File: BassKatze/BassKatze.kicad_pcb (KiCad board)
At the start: 2 copper layers, 55 x 54.9 mm, 52 parts, among them J1 Conn_01x02_Female, Q1 IRF7404, Q2 BSS138, SW1 SW_Push, U1 ATmega328-AU, U2 MSGEQ7, U3 TP4056

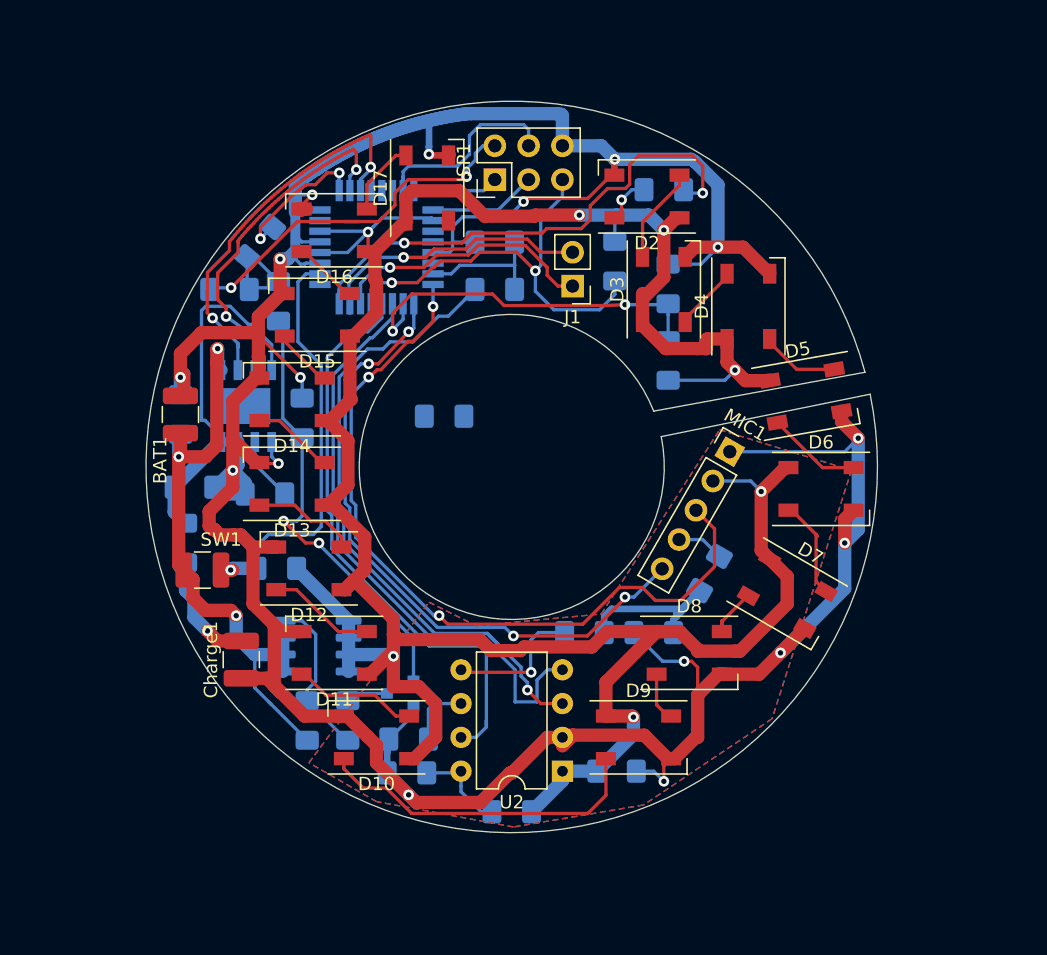
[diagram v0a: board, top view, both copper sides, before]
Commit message: use TP5400 to remove issues with isp voltage
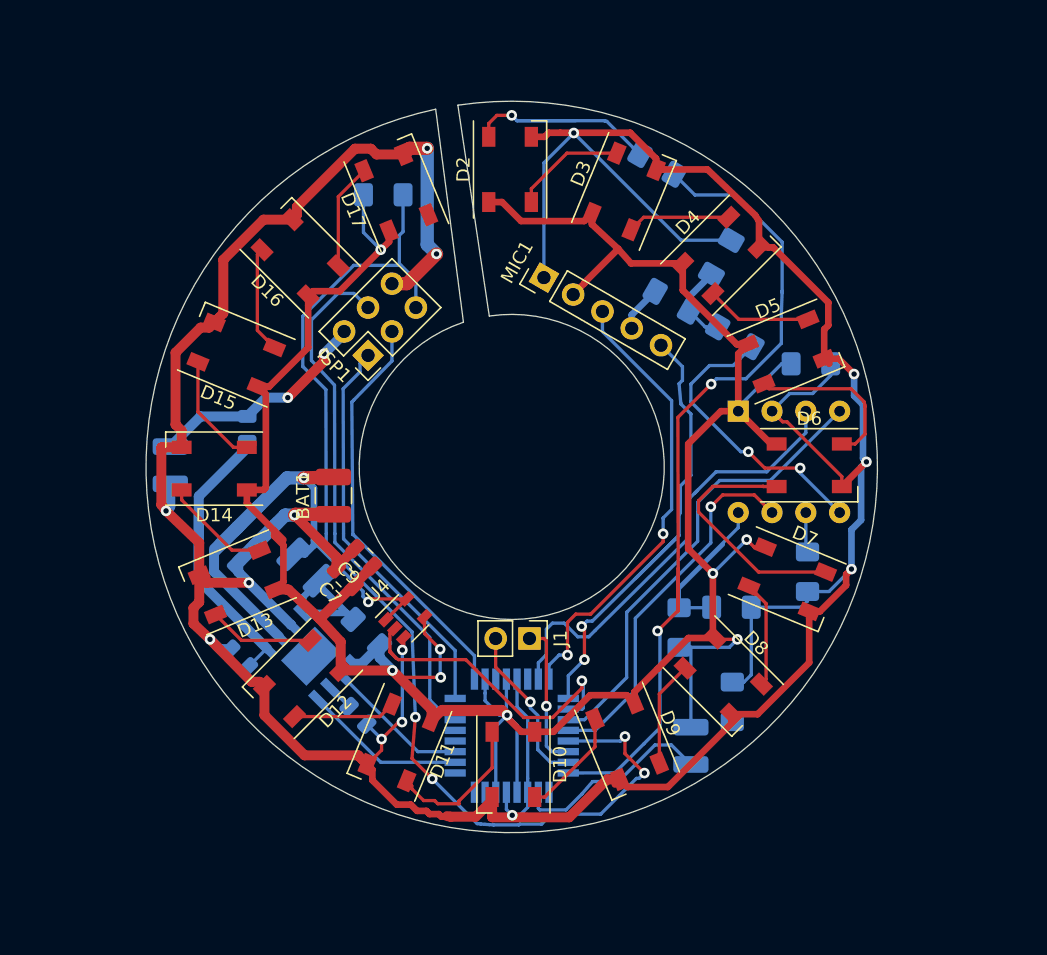
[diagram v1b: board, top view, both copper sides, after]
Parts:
- removed D18, D19: D, Diode_SMD:D_1206_3216Metric_Pad1.42x1.75mm_HandSolder
- removed Q1: IRF7404, Package_SO:SOIC-8_3.9x4.9mm_P1.27mm
- removed Q2: BSS138, Package_TO_SOT_SMD:SOT-23
- removed R10, R8: 5KOhm, Resistor_SMD:R_1206_3216Metric_Pad1.42x1.75mm_HandSolder
- removed R11, R12, R13: 10KOhm, Resistor_SMD:R_1206_3216Metric_Pad1.42x1.75mm_HandSolder
- removed R7, R9: 1KOhm, Resistor_SMD:R_1206_3216Metric_Pad1.42x1.75mm_HandSolder
- removed RProg1: 1.2kOhm, Resistor_SMD:R_1206_3216Metric_Pad1.42x1.75mm_HandSolder
- added C10: 22uF, Capacitor_SMD:C_0805_2012Metric, B.Cu at (105.7, 133.6)
- added C7: 0.1uF, Capacitor_SMD:C_0805_2012Metric, F.Cu at (114.5, 135.3)
- added C8: 22uF, Capacitor_SMD:C_0805_2012Metric, B.Cu at (107.1, 132.2)
- added C9: 47uF, Capacitor_SMD:C_0805_2012Metric, F.Cu at (115.9, 133.8)
- added L1: 10uH, Inductor_SMD:L_1210_3225Metric, B.Cu at (111.6, 134.6)
- added U4: TS5A3166DBVR, Package_TO_SOT_SMD:SOT-23-5, F.Cu at (119.0, 138.4)
- C1: footprint Resistor_SMD:R_1206_3216Metric_Pad1.42x1.75mm_HandSolder -> Capacitor_SMD:C_0805_2012Metric
- C2: value 10uF -> 0.1uF; footprint Resistor_SMD:R_1206_3216Metric_Pad1.42x1.75mm_HandSolder -> Capacitor_SMD:C_0805_2012Metric
- Charge1, SW1, U2: moved to B.Cu
- D1: value D -> 3A 20V; footprint Diode_SMD:D_1206_3216Metric_Pad1.42x1.75mm_HandSolder -> Diode_SMD:D_1206_3216Metric
- R1: value 0.4Ohm -> 0.2Ohm; footprint Resistor_SMD:R_1206_3216Metric_Pad1.42x1.75mm_HandSolder -> Resistor_SMD:R_0805_2012Metric
- R4: value 10KOhm -> 1.2KOhm; footprint Resistor_SMD:R_1206_3216Metric_Pad1.42x1.75mm_HandSolder -> Resistor_SMD:R_0805_2012Metric
- U3: value TP4056 -> TP5400
- moved SW1 39.0 mm to (140.5, 148.0), turned to 270 degrees
- moved U1 38.1 mm to (127.0, 147.2), turned to 90 degrees
- moved C5 33.9 mm to (149.5, 119.3)
- moved C6 32.5 mm to (149.2, 134.9), turned to 270 degrees
- moved R15 30.5 mm to (143.6, 144.7), turned to 270 degrees
- moved U2 30.1 mm to (144.0, 122.8), turned to 270 degrees
- moved R2 28.6 mm to (142.7, 111.3), turned to 240 degrees
- moved C4 27.4 mm to (143.5, 137.5), turned to 0 degrees
- moved J1 26.7 mm to (128.3, 139.9), turned to 270 degrees
- moved C3 24.9 mm to (143.8, 117.2), turned to 150 degrees
- moved R6 20.6 mm to (139.1, 114.6), turned to 150 degrees
- moved U3 19.4 mm to (111.9, 141.2), turned to 135 degrees
- moved MIC1 19.1 mm to (129.4, 112.8), turned to 60 degrees
- moved R3 18.7 mm to (139.6, 139.1), turned to 270 degrees
- moved R5 18.1 mm to (117.3, 106.6), turned to 0 degrees
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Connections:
- C1 pad 1: Net-(C1-Pad1) -> BAT-
- C1 pad 2: BAT- -> Net-(C1-Pad2)
- Charge1 pad 2: 5V_IN -> 5V_Flash
- D1 pad 2: Button -> Net-(D1-Pad2)
- D17 pad 4: Net-(D17-Pad4) -> (no net)
- R1 pad 1: 5V_IN -> Net-(C1-Pad2)
- R1 pad 2: Net-(C1-Pad1) -> 5V_Flash
- R4 pad 1: Net-(Q1-Pad4) -> BAT-
- R4 pad 2: BAT+ -> Net-(R4-Pad2)
- R5 pad 1: Reset -> PWR
- R5 pad 2: PWR -> Reset
- SW1 pad 1: BAT+ -> PWR
- U1 pad 1: Net-(U1-Pad1) -> (no net)
- U1 pad 10: CHRG -> STDBY
- U1 pad 11: STDBY -> CHRG
- U1 pad 12: Net-(U1-Pad12) -> (no net)
- U1 pad 13: Net-(U1-Pad13) -> (no net)
- U1 pad 14: Net-(U1-Pad14) -> (no net)
- U1 pad 19: Net-(U1-Pad19) -> (no net)
- U1 pad 20: Net-(U1-Pad20) -> PWR
- U1 pad 22: Net-(U1-Pad22) -> (no net)
- U1 pad 23: Net-(R10-Pad2) -> RAW_Spectrum
- U1 pad 26: Net-(R7-Pad1) -> BAT+_Switched
- U1 pad 7: Net-(U1-Pad7) -> (no net)
- U1 pad 8: Net-(U1-Pad8) -> (no net)
- U1 pad 9: PWR_HOLD -> (no net)
- U3 pad 1: BAT- -> PWR
- U3 pad 2: Net-(RProg1-Pad1) -> CHRG
- U3 pad 3: BAT- -> Net-(R4-Pad2)
- U3 pad 4: Net-(C1-Pad1) -> STDBY
- U3 pad 5: BAT+ -> Net-(C1-Pad2)
- U3 pad 6: STDBY -> BAT+
- U3 pad 7: CHRG -> BAT-
- U3 pad 8: Net-(C1-Pad1) -> Net-(D1-Pad2)
- U3 pad 9: Net-(U3-Pad9) -> (no net)
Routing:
- net Reset: track 32.4 -> 85.1 mm, vias 2 -> 4
- net Net-(Q2-Pad1): track 33.5 -> 0.00 mm, vias 2 -> 0
- net Net-(R7-Pad1): track 28.2 -> 0.00 mm, vias 2 -> 0
- net Net-(C1-Pad1): track 28.0 -> 0.00 mm
- net Net-(C1-Pad2): track 0.00 -> 26.4 mm
- net Gain_Select: track 59.3 -> 34.6 mm, vias 3 -> 2
- net Net-(R14-Pad2): track 39.2 -> 63.6 mm
- net MOSI: track 15.6 -> 39.9 mm
- net BAT+_Switched: track 0.00 -> 23.8 mm, vias 0 -> 1
- net MISO: track 6.43 -> 30.0 mm
- net SCK: track 8.12 -> 31.2 mm
- net BAT-: track 285.3 -> 306.6 mm, vias 16 -> 14
- net RAW_Spectrum: track 51.8 -> 34.0 mm, vias 1 -> 0
- net STDBY: track 29.8 -> 12.3 mm, vias 2 -> 0
- net Net-(D10-Pad2): track 25.1 -> 8.17 mm
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- removed copper zone on B.Cu, net BAT-
- removed copper zone on F.Cu, net BAT-
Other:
- board size 55 x 54.9 mm -> 55 x 55 mm
- board text removed: "BassKatze Rev 0.4"

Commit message: update of the layout
Signed-off-by: Kai Boernert <kai-boernert@visiongamestudios.de>
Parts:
- C3, C4, C5, C6, R14, R15, R2, R3, R5, R6: footprint Resistor_SMD:R_1206_3216Metric_Pad1.42x1.75mm_HandSolder -> Resistor_SMD:R_0805_2012Metric_Pad1.15x1.40mm_HandSolder
- R1: footprint Resistor_SMD:R_0805_2012Metric -> Resistor_SMD:R_1206_3216Metric_Pad1.42x1.75mm_HandSolder
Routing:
- net PWR: track 227.0 -> 237.6 mm
- net BAT-: track 306.6 -> 309.7 mm, vias 14 -> 15
- net RAW_Spectrum: track 34.0 -> 32.0 mm
- net Attack_Select: track 36.5 -> 35.6 mm
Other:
- board text added: "BassKatze 0.6"

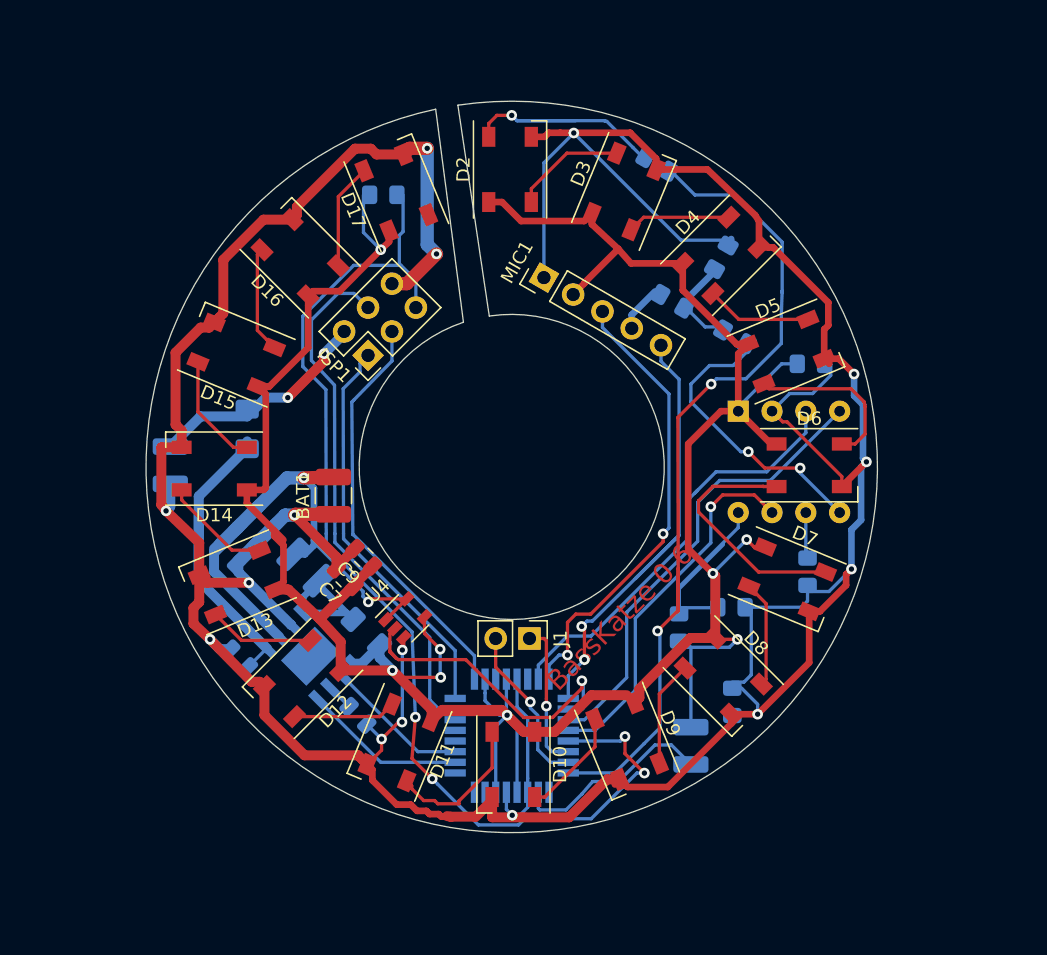
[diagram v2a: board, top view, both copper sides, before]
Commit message: 0.7 low voltage cutoff mosfet
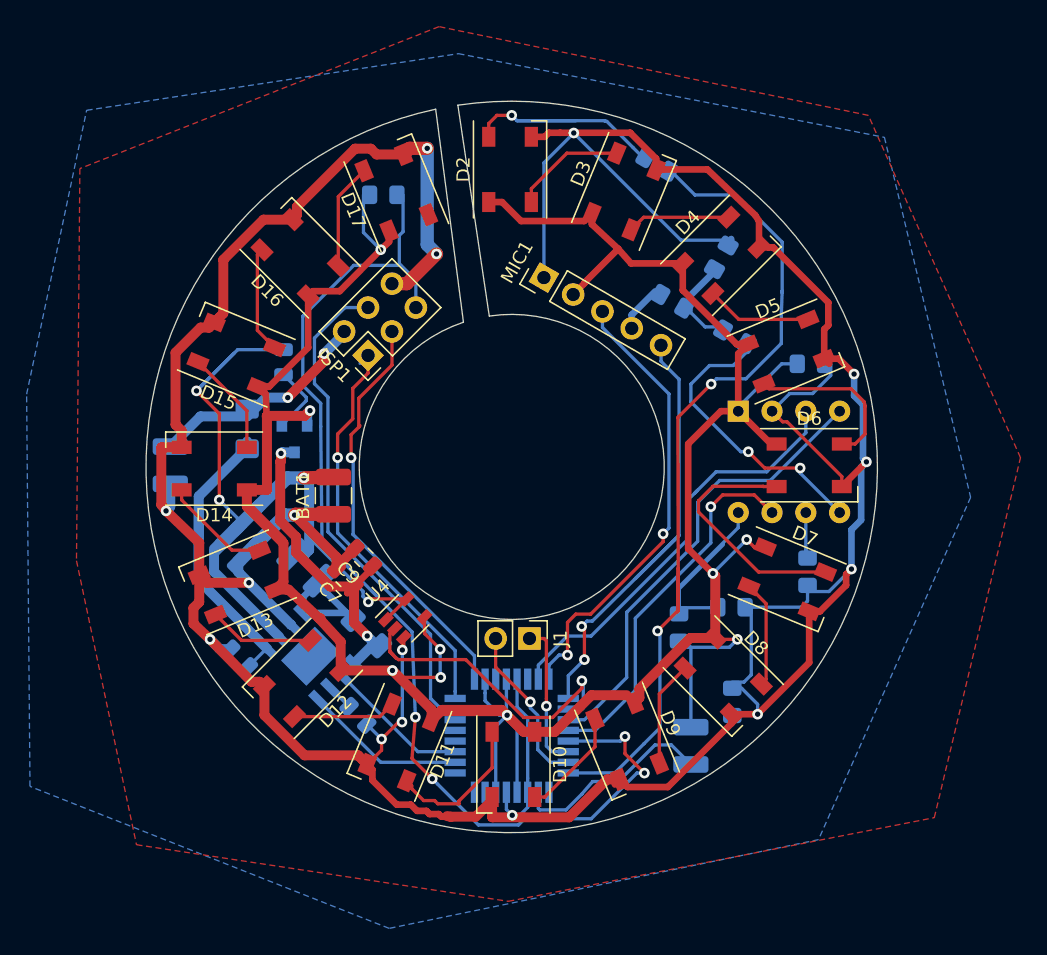
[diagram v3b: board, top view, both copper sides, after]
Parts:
- added Q1: Q_PMOS_GDS, Package_TO_SOT_SMD:SOT-23, B.Cu at (110.7, 124.9)
- added e: R, Resistor_SMD:R_0805_2012Metric, B.Cu at (109.9, 119.1)
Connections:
- C7 pad 1: PWR -> Net-(C7-Pad1)
- C9 pad 1: PWR -> Net-(C7-Pad1)
- D1 pad 1: PWR -> Net-(C7-Pad1)
- U3 pad 1: PWR -> Net-(C7-Pad1)
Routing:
- net Net-(C7-Pad1): track 0.00 -> 25.1 mm, vias 0 -> 2
- net BAT+: track 38.4 -> 61.3 mm, vias 2 -> 4
- net Net-(10K1-Pad2): track 0.00 -> 5.31 mm
- net PWR: track 237.6 -> 241.3 mm, vias 8 -> 9
- net MOSI: track 39.9 -> 37.8 mm
- net MISO: track 30.0 -> 31.2 mm, vias 0 -> 1
- net Reset: track 85.2 -> 85.8 mm
- net Net-(D14-Pad4): track 8.53 -> 7.94 mm
- net SCK: track 31.2 -> 31.4 mm, vias 0 -> 1
- added copper zone on B.Cu, net BAT-
- added copper zone on F.Cu, net BAT-
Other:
- board text added: "BassKatze 0.7"
- board text removed: "BassKatze 0.6"
